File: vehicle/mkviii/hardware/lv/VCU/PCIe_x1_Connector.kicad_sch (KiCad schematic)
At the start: 15 parts, among them J2 J_PCIe_x1, U3 MCP6001T-I/LT

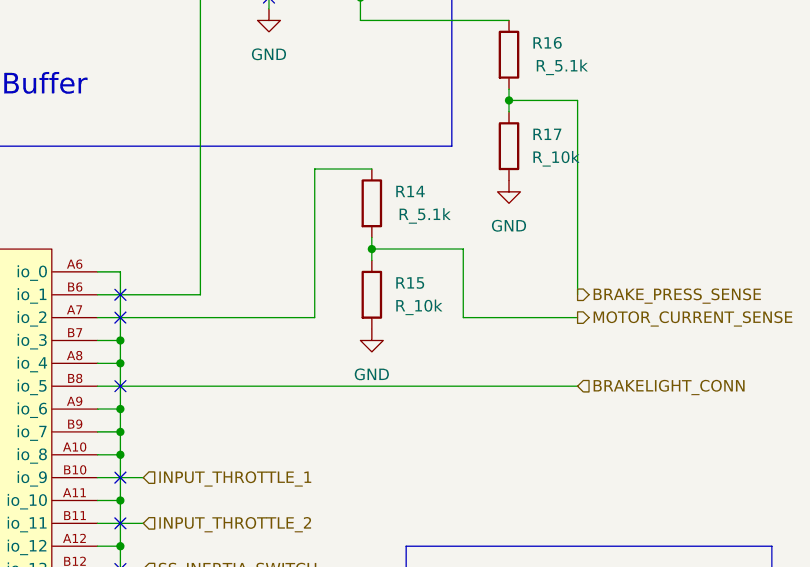
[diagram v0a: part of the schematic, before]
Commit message: Updated VCU Kicad including both schematics and layout according to changes that had been made during hardware testing: removed R15, changed R14 to 0 ohm
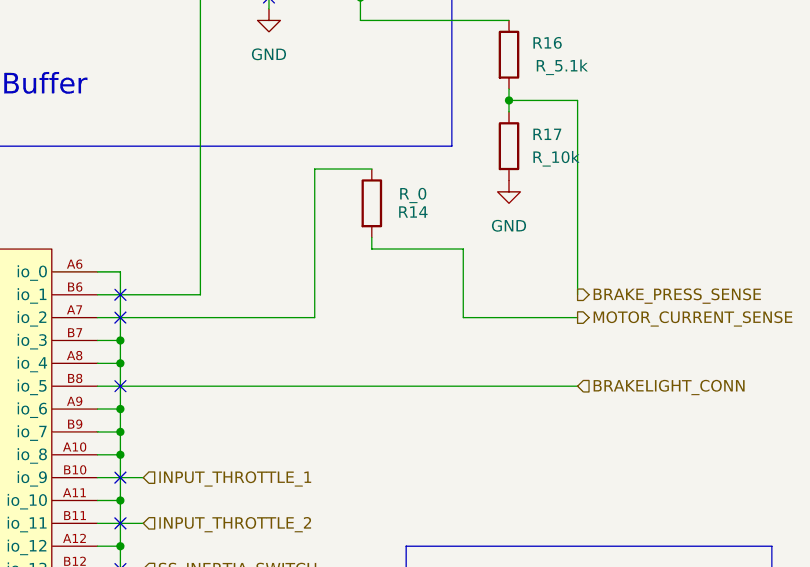
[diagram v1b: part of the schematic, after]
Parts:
- removed R15: R_10k, OEM:R_0603_1608Metric, symbol OEM:R_10k_0.1W_0603
- R14: value R_5.1k -> R_0; symbol OEM:R_5.1k_0.1W_0603 -> OEM:R_0_0.1W_0603; MPN CR0603AFX-5101EAS -> RMCF0603ZT0R00
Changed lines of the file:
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@@
 	)
 	(junction
-		(at 218.44 86.36)
-		(diameter 0)
-		(color 0 0 0 0)
-	)
-	(junction
 		(at 190.5 96.52)
 		(diameter 0)
@@
 	(wire
 		(pts
-			(xy 218.44 86.36) (xy 218.44 87.63)
-		)
-		(stroke
-			(width 0)
-			(type default)
-		)
-	)
-	(wire
-		(pts
 			(xy 187.96 121.92) (xy 193.04 121.92)
 		)
@@
 	)
 	(symbol
-		(lib_id "OEM:R_10k_0.1W_0603")
-		(at 218.44 91.44 0)
-		(unit 1)
-		(exclude_from_sim no)
-		(in_bom yes)
-		(on_board yes)
-		(dnp no)
-		(fields_autoplaced yes)
-		(property "Reference" "R15"
-			(at 220.98 90.1699 0)
-			(effects
-				(font
-					(size 1.27 1.27)
-				)
-				(justify left)
-			)
-		)
-		(property "Value" "R_10k"
-			(at 220.98 92.7099 0)
-			(effects
-				(font
-					(size 1.27 1.27)
-				)
-				(justify left)
-			)
-		)
-		(property "Footprint" "OEM:R_0603_1608Metric"
-			(at 216.662 91.44 90)
-			(effects
-				(font
-					(size 1.27 1.27)
-				)
-				(hide yes)
-			)
-		)
-		(property "Datasheet" "https://www.mouser.com/datasheet/3/1099/1/SEI-RMCF_RMCP.pdf"
-			(at 218.44 91.44 0)
-			(effects
-				(font
-					(size 1.27 1.27)
-				)
-				(hide yes)
-			)
-		)
-		(property "Description" "RES 10K OHM 1% 1/10W 0603"
-			(at 218.44 91.44 0)
-			(effects
-				(font
-					(size 1.27 1.27)
-				)
-				(hide yes)
-			)
-		)
-		(property "MPN" "RMCF0603FT10K0"
-			(at 218.44 91.44 0)
-			(effects
-				(font
-					(size 1.27 1.27)
-				)
-				(hide yes)
-			)
-		)
-		(pin "2"
-		)
-		(pin "1"
-		)
-		(instances
-			(project "VCU"
-				(path "/ec5dd9e3-3092-4af4-bee1-94131d9ab7f8/f5075997-e0a3-4d84-b3da-8739948f4d50"
-					(reference "R15")
-					(unit 1)
-				)
-			)
-		)
-	)
-	(symbol
 		(lib_id "OEM:C_10uF_10V_0603")
 		(at 132.08 64.77 0)
@@
 	)
 	(symbol
-		(lib_id "power:GND")
-		(at 218.44 95.25 0)
-		(unit 1)
-		(exclude_from_sim no)
-		(in_bom yes)
-		(on_board yes)
-		(dnp no)
-		(fields_autoplaced yes)
-		(property "Reference" "#PWR?"
-			(at 218.44 101.6 0)
-			(effects
-				(font
-					(size 1.27 1.27)
-				)
-				(hide yes)
-			)
-		)
-		(property "Value" "GND"
-			(at 218.44 100.33 0)
-			(effects
-				(font
-					(size 1.27 1.27)
-				)
-			)
-		)
-		(property "Footprint" ""
-			(at 218.44 95.25 0)
-			(effects
-				(font
-					(size 1.27 1.27)
-				)
-				(hide yes)
-			)
-		)
-		(property "Datasheet" ""
-			(at 218.44 95.25 0)
-			(effects
-				(font
-					(size 1.27 1.27)
-				)
-				(hide yes)
-			)
-		)
-		(property "Description" "Power symbol creates a global label with name \"GND\" , ground"
-			(at 218.44 95.25 0)
-			(effects
-				(font
-					(size 1.27 1.27)
-				)
-				(hide yes)
-			)
-		)
-		(pin "1"
-		)
-		(instances
-			(project "VCU"
-				(path "/ec5dd9e3-3092-4af4-bee1-94131d9ab7f8/f5075997-e0a3-4d84-b3da-8739948f4d50"
-					(reference "#PWR?")
-					(unit 1)
-				)
-			)
-		)
-	)
-	(symbol
 		(lib_id "OEM:C_10uF_10V_0603")
 		(at 133.35 87.63 0)
@@
 	)
 	(symbol
-		(lib_id "OEM:R_5.1k_0.1W_0603")
+		(lib_id "OEM:R_0_0.1W_0603")
 		(at 218.44 81.28 0)
 		(unit 1)
@@
 		(dnp no)
 		(property "Reference" "R14"
-			(at 220.98 80.0099 0)
+			(at 223.012 82.296 0)
 			(effects
 				(font
 					(size 1.27 1.27)
 				)
-				(justify left)
 			)
 		)
-		(property "Value" "R_5.1k"
-			(at 224.282 82.55 0)
+		(property "Value" "R_0"
+			(at 223.012 80.264 0)
 			(effects
 				(font
@@
 			)
 		)
-		(property "Datasheet" "https://www.mouser.com/datasheet/3/40/1/cr-a-as.pdf"
+		(property "Datasheet" "https://www.mouser.com/datasheet/3/1099/1/SEI-RMCF_RMCP.pdf"
 			(at 218.44 81.28 0)
 			(effects
@@
 			)
 		)
-		(property "Description" "RESA-AS 0603 5K1 1% 1/10W TC100"
+		(property "Description" "RES 0 OHM JUMPER 1/10W 0603"
 			(at 218.44 81.28 0)
 			(effects
@@
 			)
 		)
-		(property "MPN" "CR0603AFX-5101EAS"
+		(property "MPN" "RMCF0603ZT0R00"
 			(at 218.44 81.28 0)
 			(effects
